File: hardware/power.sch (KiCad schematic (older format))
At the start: 4 parts

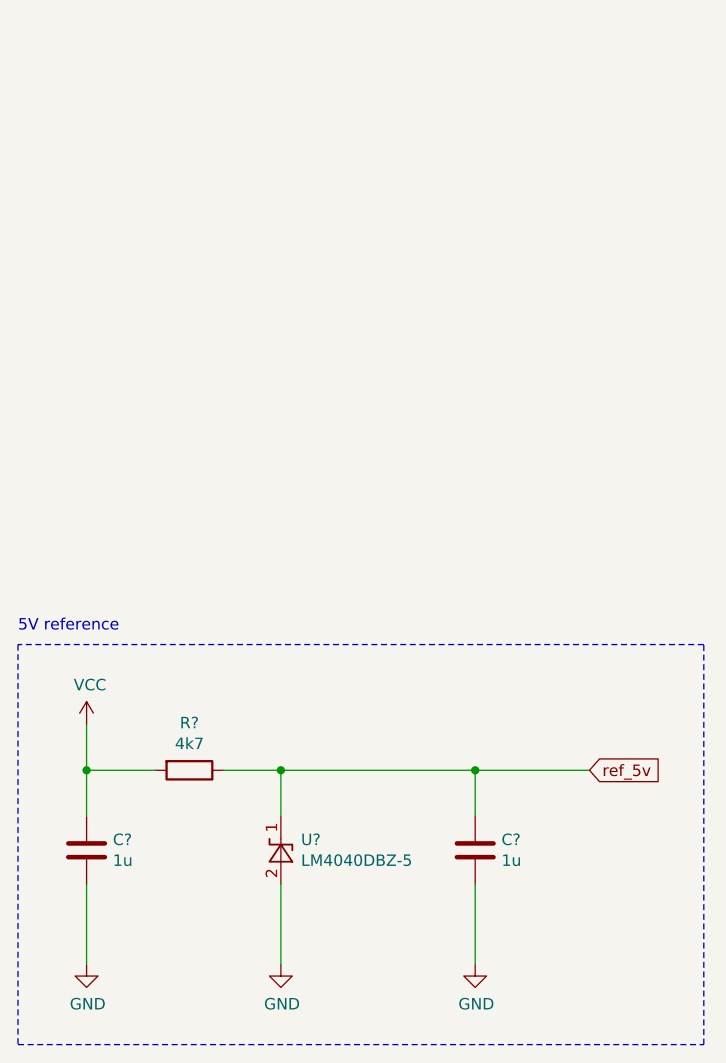
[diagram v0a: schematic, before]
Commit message: Adjust CV-ins
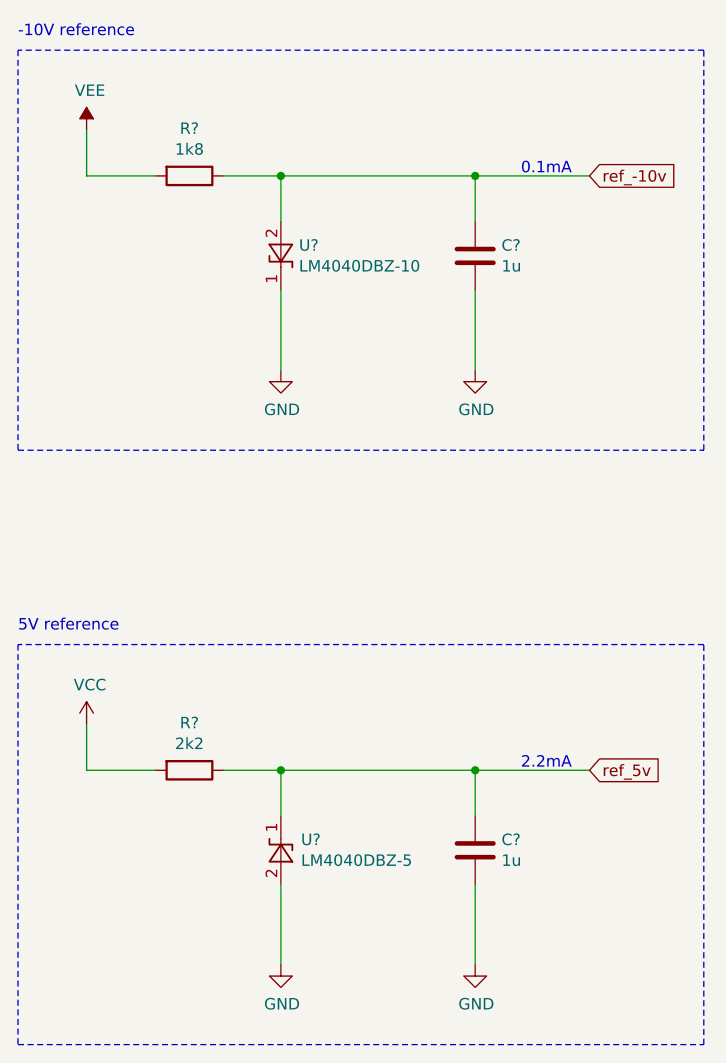
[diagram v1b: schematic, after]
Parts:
- removed C?: 1u, symbol Device:C
- added C?: 1u, symbol Device:C
- added R?: 1k8, symbol Device:R
- added U?: LM4040DBZ-10, Package_TO_SOT_SMD:SOT-23, symbol Reference_Voltage:LM4040DBZ-10
- R?: value 4k7 -> 2k2
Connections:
- net GND: now also C?.2, U?.1 (K)
- new net VEE: R?.2
- new net ref_-10v: C?.1, R?.1, U?.2 (A)
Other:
- note added: "-10V reference"
- note added: "0.1mA"
- note added: "2.2mA"
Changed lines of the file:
@@
-	1    0    0    -1
-$EndComp
-$Comp
-L power:GND #PWR?
-U 1 1 5FCB3D42
-P 7250 5500
-F 0 "#PWR?" H 7250 5250 50  0001 C CNN
-F 1 "GND" H 7255 5327 50  0000 C CNN
-F 2 "" H 7250 5500 50  0001 C CNN
-F 3 "" H 7250 5500 50  0001 C CNN
-	1    7250 5500
-	1    0    0    -1
-$EndComp
-$Comp
-L Device:C C?
-U 1 1 5FCB5486
-P 7250 5000
-F 0 "C?" H 7365 5046 50  0000 L CNN
-F 1 "1u" H 7365 4955 50  0000 L CNN
-F 2 "" H 7288 4850 50  0001 C CNN
-F 3 "~" H 7250 5000 50  0001 C CNN
-	1    7250 5000
 	1    0    0    -1
 $EndComp
@@
 	7250 4650 7550 4650
 Wire Wire Line
-	7250 4650 7250 4850
-Connection ~ 7250 4650
-Wire Wire Line
 	8100 4650 8100 4850
-Wire Wire Line
-	7250 5150 7250 5500
 $Comp
 L power:GND #PWR?
@@
 P 7700 4650
 F 0 "R?" V 7493 4650 50  0000 C CNN
-F 1 "4k7" V 7584 4650 50  0000 C CNN
+F 1 "2k2" V 7584 4650 50  0000 C CNN
 F 2 "" V 7630 4650 50  0001 C CNN
 F 3 "~" H 7700 4650 50  0001 C CNN
@@
 Text Notes 6950 4050 0    50   ~ 0
 5V reference
+Wire Wire Line
+	7250 1850 7250 2050
+Wire Wire Line
+	7250 2050 7550 2050
+Wire Wire Line
+	8100 2050 8100 2250
+$Comp
+L power:GND #PWR?
+U 1 1 5FD4341E
+P 8100 2900
+F 0 "#PWR?" H 8100 2650 50  0001 C CNN
+F 1 "GND" H 8105 2727 50  0000 C CNN
+F 2 "" H 8100 2900 50  0001 C CNN
+F 3 "" H 8100 2900 50  0001 C CNN
+	1    8100 2900
+	1    0    0    -1
+$EndComp
+Wire Wire Line
+	8100 2550 8100 2900
+Wire Wire Line
+	7850 2050 8100 2050
+$Comp
+L Device:R R?
+U 1 1 5FD43427
+P 7700 2050
+F 0 "R?" V 7493 2050 50  0000 C CNN
+F 1 "1k8" V 7584 2050 50  0000 C CNN
+F 2 "" V 7630 2050 50  0001 C CNN
+F 3 "~" H 7700 2050 50  0001 C CNN
+F 4 "0-2mA, 3k3 - 7k ohm" V 7700 2050 50  0001 C CNN "Note"
+	1    7700 2050
+	0    1    1    0
+$EndComp
+$Comp
+L Device:C C?
+U 1 1 5FD4342D
+P 8950 2400
+F 0 "C?" H 9065 2446 50  0000 L CNN
+F 1 "1u" H 9065 2355 50  0000 L CNN
+F 2 "" H 8988 2250 50  0001 C CNN
+F 3 "~" H 8950 2400 50  0001 C CNN
+	1    8950 2400
+	1    0    0    -1
+$EndComp
+Wire Wire Line
+	8100 2050 8950 2050
+Wire Wire Line
+	8950 2050 8950 2250
+Connection ~ 8100 2050
+$Comp
+L power:GND #PWR?
+U 1 1 5FD43436
+P 8950 2900
+F 0 "#PWR?" H 8950 2650 50  0001 C CNN
+F 1 "GND" H 8955 2727 50  0000 C CNN
+F 2 "" H 8950 2900 50  0001 C CNN
+F 3 "" H 8950 2900 50  0001 C CNN
+	1    8950 2900
+	1    0    0    -1
+$EndComp
+Wire Wire Line
+	8950 2550 8950 2900
+Text GLabel 9450 2050 2    50   Input ~ 0
+ref_-10v
+Connection ~ 8950 2050
+Wire Wire Line
+	8950 2050 9450 2050
+Wire Notes Line
+	6950 1500 6950 3250
+Wire Notes Line
+	6950 3250 9950 3250
+Wire Notes Line
+	9950 3250 9950 1500
+Wire Notes Line
+	9950 1500 6950 1500
+Text Notes 6950 1450 0    50   ~ 0
+-10V reference
+$Comp
+L power:VEE #PWR?
+U 1 1 5FD437B3
+P 7250 1850
+F 0 "#PWR?" H 7250 1700 50  0001 C CNN
+F 1 "VEE" H 7265 2023 50  0000 C CNN
+F 2 "" H 7250 1850 50  0001 C CNN
+F 3 "" H 7250 1850 50  0001 C CNN
+	1    7250 1850
+	1    0    0    -1
+$EndComp
+$Comp
+L Reference_Voltage:LM4040DBZ-10 U?
+U 1 1 5FD44CC9
+P 8100 2400
+F 0 "U?" V 8054 2479 50  0000 L CNN
+F 1 "LM4040DBZ-10" V 8145 2479 50  0000 L CNN
+F 2 "Package_TO_SOT_SMD:SOT-23" H 8100 2200 50  0001 C CIN
+F 3 "http://www.ti.com/lit/ds/symlink/lm4040-n.pdf" H 8100 2400 50  0001 C CIN
+	1    8100 2400
+	0    1    1    0
+$EndComp
+Text Notes 9150 2050 0    50   ~ 0
+0.1mA
+Text Notes 9150 4650 0    50   ~ 0
+2.2mA
 $EndSCHEMATC
